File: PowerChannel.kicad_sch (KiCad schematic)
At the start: 15 parts, among them J3 Screw_Terminal_01x04, Q4 2N7002, Q5 NTF6P02, Q6 2N7002, U13 INA219xID

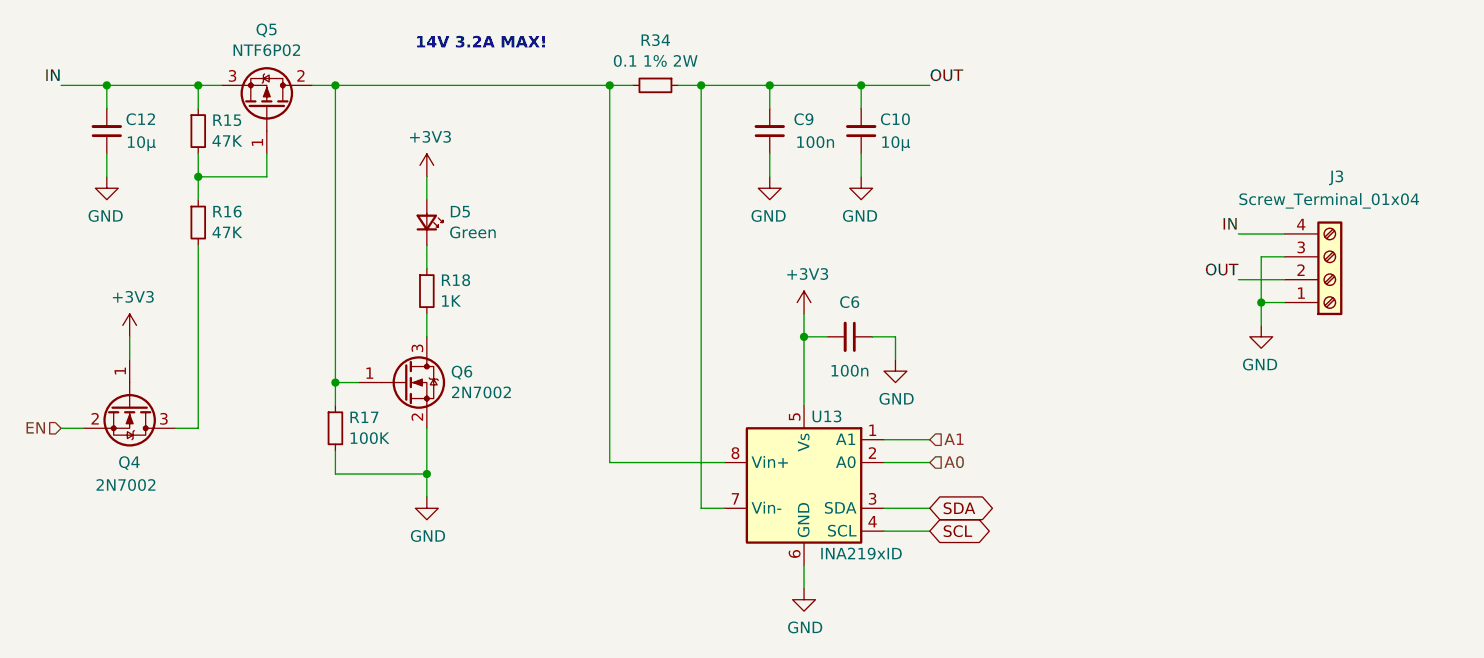
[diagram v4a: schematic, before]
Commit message: Schematic: Re-annotate symbol references
Fill in schematic symbol reference designators, with reset
existing annotations.

Signed-off-by: Geert Uytterhoeven <geert@linux-m68k.org>
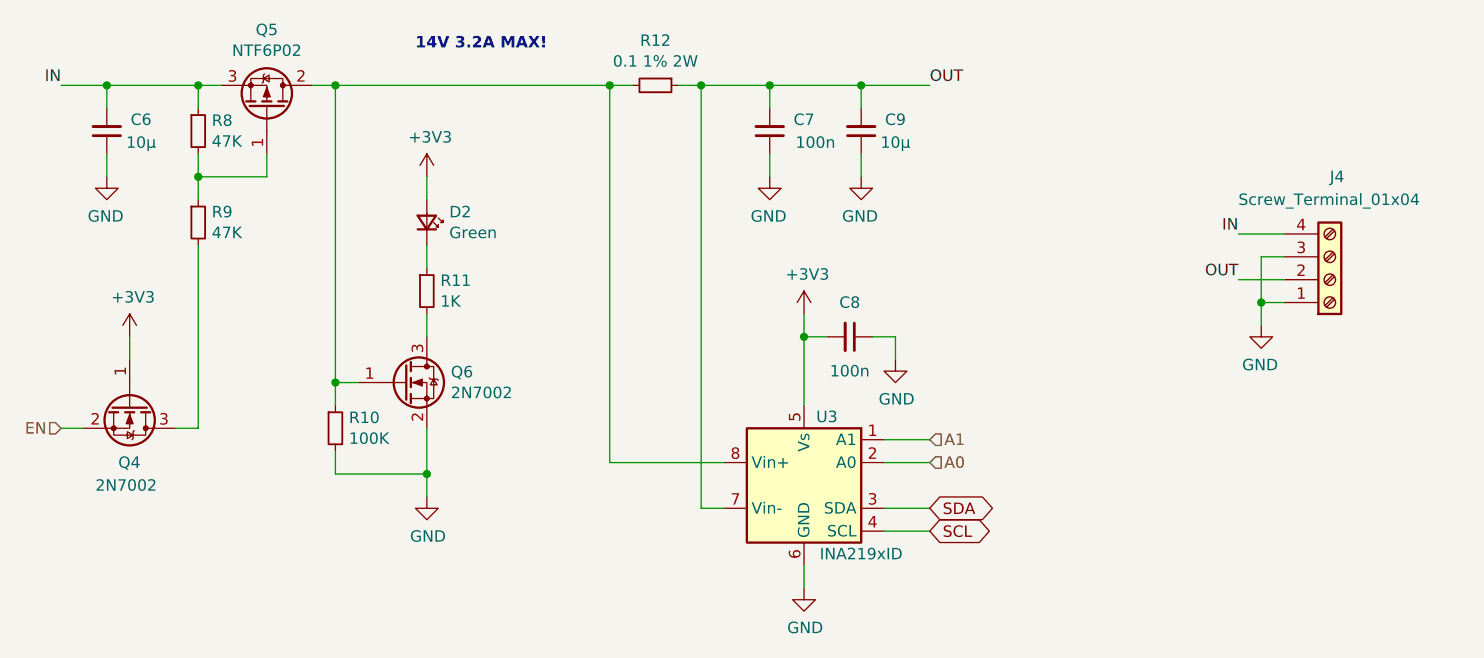
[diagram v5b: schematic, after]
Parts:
- renumbered C12 to C6, C9 to C7, C6 to C8, C10 to C9, D5 to D2, J3 to J4, R17 to R10, R18 to R11, R34 to R12, R15 to R8, R16 to R9, U13 to U3
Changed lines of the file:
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@@
   (symbol (lib_id "Device:R_Small") (at 53.34 40.64 0)
     (in_bom yes) (on_board yes)
-    (property "Reference" "R16" (id 0) (at 54.8386 39.4716 0)
+    (property "Reference" "R9" (id 0) (at 54.8386 39.4716 0)
       (effects (font (size 1.27 1.27)) (justify left))
     )
@@
   (symbol (lib_id "Device:R_Small") (at 53.34 30.48 0)
     (in_bom yes) (on_board yes)
-    (property "Reference" "R15" (id 0) (at 54.8386 29.3116 0)
+    (property "Reference" "R8" (id 0) (at 54.8386 29.3116 0)
       (effects (font (size 1.27 1.27)) (justify left))
     )
@@
   (symbol (lib_id "Device:R_Small") (at 68.58 63.5 0)
     (in_bom yes) (on_board yes)
-    (property "Reference" "R17" (id 0) (at 70.0786 62.3316 0)
+    (property "Reference" "R10" (id 0) (at 70.0786 62.3316 0)
       (effects (font (size 1.27 1.27)) (justify left))
     )
@@
   (symbol (lib_id "power:GND") (at 78.74 71.12 0)
     (in_bom yes) (on_board yes)
-    (property "Reference" "#PWR012" (id 0) (at 78.74 77.47 0)
+    (property "Reference" "#PWR028" (id 0) (at 78.74 77.47 0)
       (effects (font (size 1.27 1.27)) hide)
     )
@@
   (symbol (lib_id "Device:R_Small") (at 78.74 48.26 0)
     (in_bom yes) (on_board yes)
-    (property "Reference" "R18" (id 0) (at 80.2386 47.0916 0)
+    (property "Reference" "R11" (id 0) (at 80.2386 47.0916 0)
       (effects (font (size 1.27 1.27)) (justify left))
     )
@@
   (symbol (lib_id "power:+3V3") (at 78.74 35.56 0)
     (in_bom yes) (on_board yes)
-    (property "Reference" "#PWR011" (id 0) (at 78.74 39.37 0)
+    (property "Reference" "#PWR027" (id 0) (at 78.74 39.37 0)
       (effects (font (size 1.27 1.27)) hide)
     )
@@
   (symbol (lib_id "Connector:Screw_Terminal_01x04") (at 179.07 46.99 0) (mirror x)
     (in_bom yes) (on_board yes)
-    (property "Reference" "J3" (id 0) (at 179.07 35.56 0)
+    (property "Reference" "J4" (id 0) (at 179.07 35.56 0)
       (effects (font (size 1.27 1.27)) (justify left))
     )
@@
   (symbol (lib_id "power:GND") (at 171.45 52.07 0) (mirror y)
     (in_bom yes) (on_board yes)
-    (property "Reference" "#PWR013" (id 0) (at 171.45 58.42 0)
+    (property "Reference" "#PWR034" (id 0) (at 171.45 58.42 0)
       (effects (font (size 1.27 1.27)) hide)
     )
@@
   (symbol (lib_id "Device:LED_Small") (at 78.74 40.64 270) (mirror x)
     (in_bom yes) (on_board yes)
-    (property "Reference" "D5" (id 0) (at 81.2292 39.4716 90)
+    (property "Reference" "D2" (id 0) (at 81.2292 39.4716 90)
       (effects (font (size 1.27 1.27)) (justify left))
     )
@@
   (symbol (lib_id "Device:R_Small") (at 104.14 25.4 270)
     (in_bom yes) (on_board yes)
-    (property "Reference" "R34" (id 0) (at 104.14 20.4216 90))
+    (property "Reference" "R12" (id 0) (at 104.14 20.4216 90))
     (property "Value" "0.1 1% 2W" (id 1) (at 104.14 22.733 90))
     (property "Footprint" "Resistor_SMD:R_2512_6332Metric_Pad1.52x3.35mm_HandSolder" (id 2) (at 104.14 25.4 0)
@@
   (symbol (lib_id "power:GND") (at 120.65 81.28 0)
     (in_bom yes) (on_board yes)
-    (property "Reference" "#PWR0110" (id 0) (at 120.65 87.63 0)
+    (property "Reference" "#PWR031" (id 0) (at 120.65 87.63 0)
       (effects (font (size 1.27 1.27)) hide)
     )
@@
   (symbol (lib_id "power:+3V3") (at 120.65 50.8 0)
     (in_bom yes) (on_board yes)
-    (property "Reference" "#PWR0111" (id 0) (at 120.65 54.61 0)
+    (property "Reference" "#PWR030" (id 0) (at 120.65 54.61 0)
       (effects (font (size 1.27 1.27)) hide)
     )
@@
   (symbol (lib_id "Device:C_Small") (at 125.73 53.34 270)
     (in_bom yes) (on_board yes)
-    (property "Reference" "C6" (id 0) (at 125.73 49.53 90))
+    (property "Reference" "C8" (id 0) (at 125.73 49.53 90))
     (property "Value" "100n" (id 1) (at 125.73 57.15 90))
     (property "Footprint" "Capacitor_SMD:C_0603_1608Metric_Pad1.05x0.95mm_HandSolder" (id 2) (at 125.73 53.34 0)
@@
   (symbol (lib_id "Device:C_Small") (at 116.84 30.48 180)
     (in_bom yes) (on_board yes)
-    (property "Reference" "C9" (id 0) (at 120.65 29.21 0))
+    (property "Reference" "C7" (id 0) (at 120.65 29.21 0))
     (property "Value" "100n" (id 1) (at 121.92 31.75 0))
     (property "Footprint" "Capacitor_SMD:C_0603_1608Metric_Pad1.05x0.95mm_HandSolder" (id 2) (at 116.84 30.48 0)
@@
   (symbol (lib_id "Device:C_Small") (at 127 30.48 180)
     (in_bom yes) (on_board yes)
-    (property "Reference" "C10" (id 0) (at 130.81 29.21 0))
+    (property "Reference" "C9" (id 0) (at 130.81 29.21 0))
     (property "Value" "10µ" (id 1) (at 130.81 31.75 0))
     (property "Footprint" "Capacitor_SMD:C_0805_2012Metric_Pad1.15x1.40mm_HandSolder" (id 2) (at 127 30.48 0)
@@
   (symbol (lib_id "power:GND") (at 116.84 35.56 0) (mirror y)
     (in_bom yes) (on_board yes)
-    (property "Reference" "#PWR031" (id 0) (at 116.84 41.91 0)
+    (property "Reference" "#PWR029" (id 0) (at 116.84 41.91 0)
       (effects (font (size 1.27 1.27)) hide)
     )
@@
   (symbol (lib_id "Device:C_Small") (at 43.18 30.48 180)
     (in_bom yes) (on_board yes)
-    (property "Reference" "C12" (id 0) (at 46.99 29.21 0))
+    (property "Reference" "C6" (id 0) (at 46.99 29.21 0))
     (property "Value" "10µ" (id 1) (at 46.99 31.75 0))
     (property "Footprint" "Capacitor_SMD:C_0805_2012Metric_Pad1.15x1.40mm_HandSolder" (id 2) (at 43.18 30.48 0)
@@
   (symbol (lib_id "power:GND") (at 43.18 35.56 0) (mirror y)
     (in_bom yes) (on_board yes)
-    (property "Reference" "#PWR034" (id 0) (at 43.18 41.91 0)
+    (property "Reference" "#PWR025" (id 0) (at 43.18 41.91 0)
       (effects (font (size 1.27 1.27)) hide)
     )
@@
   (symbol (lib_id "INA219:INA219xID") (at 120.65 69.85 0)
     (in_bom yes) (on_board yes)
-    (property "Reference" "U13" (id 0) (at 123.19 62.23 0))
+    (property "Reference" "U3" (id 0) (at 123.19 62.23 0))
     (property "Value" "INA219xID" (id 1) (at 127 77.47 0))
     (property "Footprint" "Package_SO:SOIC-8_3.9x4.9mm_P1.27mm" (id 2) (at 129.54 69.85 0)
@@
   (symbol (lib_id "power:GND") (at 130.81 55.88 0)
     (in_bom yes) (on_board yes)
-    (property "Reference" "#PWR044" (id 0) (at 130.81 62.23 0)
+    (property "Reference" "#PWR033" (id 0) (at 130.81 62.23 0)
       (effects (font (size 1.27 1.27)) hide)
     )
@@
   (symbol (lib_id "power:+3V3") (at 45.72 53.34 0)
     (in_bom yes) (on_board yes)
-    (property "Reference" "#PWR020" (id 0) (at 45.72 57.15 0)
-      (effects (font (size 1.27 1.27)) hide)
-    )
+    (property "Reference" "#PWR026" (id 0) (at 45.72 57.15 0)
+      (effects (font (size 1.27 1.27)) hide)
+    )

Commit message: Schematic: Update footprints
Update Capacitor, LED, and Resistor footprints to match KiCad 6.

Signed-off-by: Geert Uytterhoeven <geert@linux-m68k.org>
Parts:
- C6, C9: footprint Capacitor_SMD:C_0805_2012Metric_Pad1.15x1.40mm_HandSolder -> Capacitor_SMD:C_0805_2012Metric_Pad1.18x1.45mm_HandSolder
- C7, C8: footprint Capacitor_SMD:C_0603_1608Metric_Pad1.05x0.95mm_HandSolder -> Capacitor_SMD:C_0603_1608Metric_Pad1.08x0.95mm_HandSolder
- D2: footprint LED_SMD:LED_0603_1608Metric_Castellated -> LED_SMD:LED_0603_1608Metric_Pad1.05x0.95mm_HandSolder
- R10, R11, R8, R9: footprint Resistor_SMD:R_0603_1608Metric_Pad1.05x0.95mm_HandSolder -> Resistor_SMD:R_0603_1608Metric_Pad0.98x0.95mm_HandSolder
- R12: footprint Resistor_SMD:R_2512_6332Metric_Pad1.52x3.35mm_HandSolder -> Resistor_SMD:R_2512_6332Metric_Pad1.40x3.35mm_HandSolder
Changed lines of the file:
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@@
       (effects (font (size 1.27 1.27)) (justify left))
     )
-    (property "Footprint" "Resistor_SMD:R_0603_1608Metric_Pad1.05x0.95mm_HandSolder" (id 2) (at 53.34 40.64 0)
+    (property "Footprint" "Resistor_SMD:R_0603_1608Metric_Pad0.98x0.95mm_HandSolder" (id 2) (at 53.34 40.64 0)
       (effects (font (size 1.27 1.27)) hide)
     )
@@
       (effects (font (size 1.27 1.27)) (justify left))
     )
-    (property "Footprint" "Resistor_SMD:R_0603_1608Metric_Pad1.05x0.95mm_HandSolder" (id 2) (at 53.34 30.48 0)
+    (property "Footprint" "Resistor_SMD:R_0603_1608Metric_Pad0.98x0.95mm_HandSolder" (id 2) (at 53.34 30.48 0)
       (effects (font (size 1.27 1.27)) hide)
     )
@@
       (effects (font (size 1.27 1.27)) (justify left))
     )
-    (property "Footprint" "Resistor_SMD:R_0603_1608Metric_Pad1.05x0.95mm_HandSolder" (id 2) (at 68.58 63.5 0)
+    (property "Footprint" "Resistor_SMD:R_0603_1608Metric_Pad0.98x0.95mm_HandSolder" (id 2) (at 68.58 63.5 0)
       (effects (font (size 1.27 1.27)) hide)
     )
@@
       (effects (font (size 1.27 1.27)) (justify left))
     )
-    (property "Footprint" "Resistor_SMD:R_0603_1608Metric_Pad1.05x0.95mm_HandSolder" (id 2) (at 78.74 48.26 0)
+    (property "Footprint" "Resistor_SMD:R_0603_1608Metric_Pad0.98x0.95mm_HandSolder" (id 2) (at 78.74 48.26 0)
       (effects (font (size 1.27 1.27)) hide)
     )
@@
       (effects (font (size 1.27 1.27)) (justify left))
     )
-    (property "Footprint" "LED_SMD:LED_0603_1608Metric_Castellated" (id 2) (at 78.74 40.64 90)
+    (property "Footprint" "LED_SMD:LED_0603_1608Metric_Pad1.05x0.95mm_HandSolder" (id 2) (at 78.74 40.64 90)
       (effects (font (size 1.27 1.27)) hide)
     )
@@
     (property "Reference" "R12" (id 0) (at 104.14 20.4216 90))
     (property "Value" "0.1 1% 2W" (id 1) (at 104.14 22.733 90))
-    (property "Footprint" "Resistor_SMD:R_2512_6332Metric_Pad1.52x3.35mm_HandSolder" (id 2) (at 104.14 25.4 0)
+    (property "Footprint" "Resistor_SMD:R_2512_6332Metric_Pad1.40x3.35mm_HandSolder" (id 2) (at 104.14 25.4 0)
       (effects (font (size 1.27 1.27)) hide)
     )
@@
     (property "Reference" "C8" (id 0) (at 125.73 49.53 90))
     (property "Value" "100n" (id 1) (at 125.73 57.15 90))
-    (property "Footprint" "Capacitor_SMD:C_0603_1608Metric_Pad1.05x0.95mm_HandSolder" (id 2) (at 125.73 53.34 0)
+    (property "Footprint" "Capacitor_SMD:C_0603_1608Metric_Pad1.08x0.95mm_HandSolder" (id 2) (at 125.73 53.34 0)
       (effects (font (size 1.27 1.27)) hide)
     )
@@
     (property "Reference" "C7" (id 0) (at 120.65 29.21 0))
     (property "Value" "100n" (id 1) (at 121.92 31.75 0))
-    (property "Footprint" "Capacitor_SMD:C_0603_1608Metric_Pad1.05x0.95mm_HandSolder" (id 2) (at 116.84 30.48 0)
+    (property "Footprint" "Capacitor_SMD:C_0603_1608Metric_Pad1.08x0.95mm_HandSolder" (id 2) (at 116.84 30.48 0)
       (effects (font (size 1.27 1.27)) hide)
     )
@@
     (property "Reference" "C9" (id 0) (at 130.81 29.21 0))
     (property "Value" "10µ" (id 1) (at 130.81 31.75 0))
-    (property "Footprint" "Capacitor_SMD:C_0805_2012Metric_Pad1.15x1.40mm_HandSolder" (id 2) (at 127 30.48 0)
+    (property "Footprint" "Capacitor_SMD:C_0805_2012Metric_Pad1.18x1.45mm_HandSolder" (id 2) (at 127 30.48 0)
       (effects (font (size 1.27 1.27)) hide)
     )
@@
     (property "Reference" "C6" (id 0) (at 46.99 29.21 0))
     (property "Value" "10µ" (id 1) (at 46.99 31.75 0))
-    (property "Footprint" "Capacitor_SMD:C_0805_2012Metric_Pad1.15x1.40mm_HandSolder" (id 2) (at 43.18 30.48 0)
-      (effects (font (size 1.27 1.27)) hide)
-    )
+    (property "Footprint" "Capacitor_SMD:C_0805_2012Metric_Pad1.18x1.45mm_HandSolder" (id 2) (at 43.18 30.48 0)
+      (effects (font (size 1.27 1.27)) hide)
+    )

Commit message: Schematic: Update title and date
Power-Opto Extension Board (POX for BCU/2)

Signed-off-by: Geert Uytterhoeven <geert@linux-m68k.org>
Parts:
- renumbered C6 to C2, C7 to C3, C8 to C4, C9 to C5, D2 to D1, J4 to J3, Q4 to Q1, Q5 to Q2, Q6 to Q3, R8 to R3, R9 to R4, R10 to R5, R11 to R6, R12 to R7, U3 to U2
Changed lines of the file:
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@@
   (symbol (lib_id "Device:R_Small") (at 53.34 40.64 0)
     (in_bom yes) (on_board yes)
-    (property "Reference" "R9" (id 0) (at 54.8386 39.4716 0)
+    (property "Reference" "R4" (id 0) (at 54.8386 39.4716 0)
       (effects (font (size 1.27 1.27)) (justify left))
     )
@@
   (symbol (lib_id "Device:R_Small") (at 53.34 30.48 0)
     (in_bom yes) (on_board yes)
-    (property "Reference" "R8" (id 0) (at 54.8386 29.3116 0)
+    (property "Reference" "R3" (id 0) (at 54.8386 29.3116 0)
       (effects (font (size 1.27 1.27)) (justify left))
     )
@@
   (symbol (lib_id "Transistor_FET:IRF9540N") (at 60.96 27.94 270) (mirror x)
     (in_bom yes) (on_board yes)
-    (property "Reference" "Q5" (id 0) (at 60.96 19.2278 90))
+    (property "Reference" "Q2" (id 0) (at 60.96 19.2278 90))
     (property "Value" "NTF6P02" (id 1) (at 60.96 21.5392 90))
     (property "Footprint" "Package_TO_SOT_SMD:SOT-223-3_TabPin2" (id 2) (at 59.055 22.86 0)
@@
   (symbol (lib_id "Device:R_Small") (at 68.58 63.5 0)
     (in_bom yes) (on_board yes)
-    (property "Reference" "R10" (id 0) (at 70.0786 62.3316 0)
+    (property "Reference" "R5" (id 0) (at 70.0786 62.3316 0)
       (effects (font (size 1.27 1.27)) (justify left))
     )
@@
   (symbol (lib_id "Device:R_Small") (at 78.74 48.26 0)
     (in_bom yes) (on_board yes)
-    (property "Reference" "R11" (id 0) (at 80.2386 47.0916 0)
+    (property "Reference" "R6" (id 0) (at 80.2386 47.0916 0)
       (effects (font (size 1.27 1.27)) (justify left))
     )
@@
   (symbol (lib_id "Connector:Screw_Terminal_01x04") (at 179.07 46.99 0) (mirror x)
     (in_bom yes) (on_board yes)
-    (property "Reference" "J4" (id 0) (at 179.07 35.56 0)
+    (property "Reference" "J3" (id 0) (at 179.07 35.56 0)
       (effects (font (size 1.27 1.27)) (justify left))
     )
@@
   (symbol (lib_id "Device:LED_Small") (at 78.74 40.64 270) (mirror x)
     (in_bom yes) (on_board yes)
-    (property "Reference" "D2" (id 0) (at 81.2292 39.4716 90)
+    (property "Reference" "D1" (id 0) (at 81.2292 39.4716 90)
       (effects (font (size 1.27 1.27)) (justify left))
     )
@@
   (symbol (lib_id "Transistor_FET:2N7002") (at 45.72 60.96 270)
     (in_bom yes) (on_board yes)
-    (property "Reference" "Q4" (id 0) (at 44.45 67.31 90)
+    (property "Reference" "Q1" (id 0) (at 44.45 67.31 90)
       (effects (font (size 1.27 1.27)) (justify left))
     )
@@
   (symbol (lib_id "Transistor_FET:2N7002") (at 76.2 58.42 0)
     (in_bom yes) (on_board yes)
-    (property "Reference" "Q6" (id 0) (at 81.407 57.2516 0)
+    (property "Reference" "Q3" (id 0) (at 81.407 57.2516 0)
       (effects (font (size 1.27 1.27)) (justify left))
     )
@@
   (symbol (lib_id "Device:R_Small") (at 104.14 25.4 270)
     (in_bom yes) (on_board yes)
-    (property "Reference" "R12" (id 0) (at 104.14 20.4216 90))
+    (property "Reference" "R7" (id 0) (at 104.14 20.4216 90))
     (property "Value" "0.1 1% 2W" (id 1) (at 104.14 22.733 90))
     (property "Footprint" "Resistor_SMD:R_2512_6332Metric_Pad1.40x3.35mm_HandSolder" (id 2) (at 104.14 25.4 0)
@@
   (symbol (lib_id "Device:C_Small") (at 125.73 53.34 270)
     (in_bom yes) (on_board yes)
-    (property "Reference" "C8" (id 0) (at 125.73 49.53 90))
+    (property "Reference" "C4" (id 0) (at 125.73 49.53 90))
     (property "Value" "100n" (id 1) (at 125.73 57.15 90))
     (property "Footprint" "Capacitor_SMD:C_0603_1608Metric_Pad1.08x0.95mm_HandSolder" (id 2) (at 125.73 53.34 0)
@@
   (symbol (lib_id "Device:C_Small") (at 116.84 30.48 180)
     (in_bom yes) (on_board yes)
-    (property "Reference" "C7" (id 0) (at 120.65 29.21 0))
+    (property "Reference" "C3" (id 0) (at 120.65 29.21 0))
     (property "Value" "100n" (id 1) (at 121.92 31.75 0))
     (property "Footprint" "Capacitor_SMD:C_0603_1608Metric_Pad1.08x0.95mm_HandSolder" (id 2) (at 116.84 30.48 0)
@@
   (symbol (lib_id "Device:C_Small") (at 127 30.48 180)
     (in_bom yes) (on_board yes)
-    (property "Reference" "C9" (id 0) (at 130.81 29.21 0))
+    (property "Reference" "C5" (id 0) (at 130.81 29.21 0))
     (property "Value" "10µ" (id 1) (at 130.81 31.75 0))
     (property "Footprint" "Capacitor_SMD:C_0805_2012Metric_Pad1.18x1.45mm_HandSolder" (id 2) (at 127 30.48 0)
@@
   (symbol (lib_id "Device:C_Small") (at 43.18 30.48 180)
     (in_bom yes) (on_board yes)
-    (property "Reference" "C6" (id 0) (at 46.99 29.21 0))
+    (property "Reference" "C2" (id 0) (at 46.99 29.21 0))
     (property "Value" "10µ" (id 1) (at 46.99 31.75 0))
     (property "Footprint" "Capacitor_SMD:C_0805_2012Metric_Pad1.18x1.45mm_HandSolder" (id 2) (at 43.18 30.48 0)
@@
   (symbol (lib_id "INA219:INA219xID") (at 120.65 69.85 0)
     (in_bom yes) (on_board yes)
-    (property "Reference" "U3" (id 0) (at 123.19 62.23 0))
+    (property "Reference" "U2" (id 0) (at 123.19 62.23 0))
     (property "Value" "INA219xID" (id 1) (at 127 77.47 0))
     (property "Footprint" "Package_SO:SOIC-8_3.9x4.9mm_P1.27mm" (id 2) (at 129.54 69.85 0)
